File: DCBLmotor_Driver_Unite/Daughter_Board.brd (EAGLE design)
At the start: 99.8 x 72.3 mm, 40 parts, among them CN1 DF11-16DP-2DSA, CN2 26-01-3115, CN3 39-28-1023, IC1 IR25750LPBF, IC2 IR25750LPBF, IC3 IR25750LPBF, IC4 DRV8320SRTVT

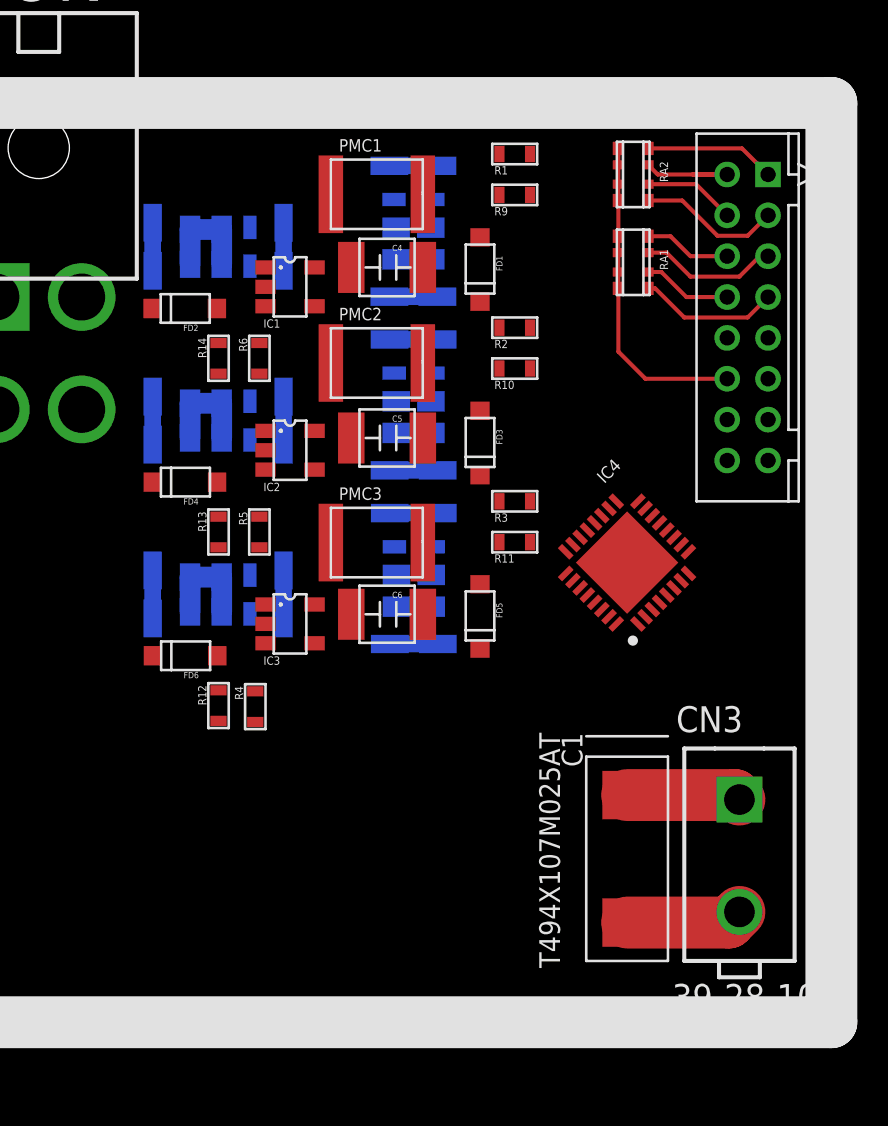
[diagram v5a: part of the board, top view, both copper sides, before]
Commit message: Build around FET
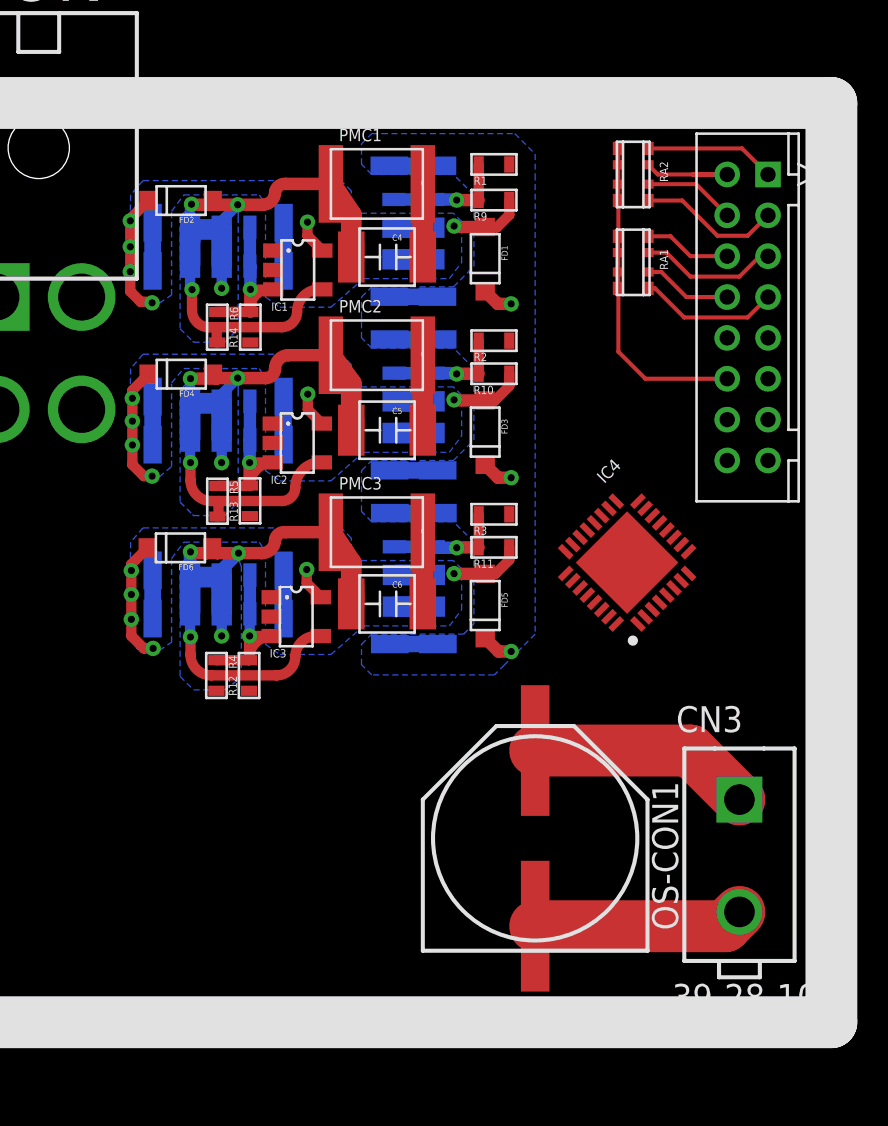
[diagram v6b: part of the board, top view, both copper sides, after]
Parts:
- removed C1: T494X107M025AT, KEMET:T494_X
- added OS-CON1: 50SVPF68M, OS-CON:F12
- moved FD6 5.29 mm to (34.5, 46.2)
- moved FD2 5.29 mm to (34.6, 63.2)
- moved FD4 5.29 mm to (34.6, 54.7)
- moved R5 1.59 mm to (39.5, 48.5)
- moved R6 1.59 mm to (39.6, 57.0)
- moved R4 1.55 mm to (39.5, 40.0)
- moved R14 1.53 mm to (37.9, 57.0), turned to 90 degrees
- moved R13 1.50 mm to (37.9, 48.5), turned to 90 degrees
- moved R12 1.48 mm to (37.9, 40.0), turned to 90 degrees
- moved R2 1.20 mm to (51.5, 56.4)
- moved R3 1.20 mm to (51.5, 47.9)
- moved R1 1.14 mm to (51.5, 65.0)
- moved R10 1.05 mm to (51.5, 54.7)
- moved R11 1.05 mm to (51.5, 46.2)
- moved R9 1.05 mm to (51.5, 63.2)
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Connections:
- removed net N$6: IC1.P$3, R14.P$2
- net GND: now also IC1.P$4, OS-CON1.P$-, R14.P$1; no longer C1.P$2
- net N$4: now also IC1.P$3, R14.P$2
- net VCC: now also OS-CON1.P$+; no longer C1.P$+
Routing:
- net GND: track 20.6 -> 106.7 mm, vias 0 -> 12
- net VCC: track 19.7 -> 40.5 mm, vias 0 -> 3
- net VS1: track 4.70 -> 19.6 mm, vias 0 -> 6
- net VS2: track 4.70 -> 19.5 mm, vias 0 -> 6
- net VS3: track 4.70 -> 19.3 mm, vias 0 -> 6
- net N$18: track 0.00 -> 8.53 mm, vias 0 -> 1
- net N$2: track 0.00 -> 8.48 mm, vias 0 -> 1
- net N$4: track 0.00 -> 8.35 mm, vias 0 -> 1
- net N$21: track 0.00 -> 5.90 mm, vias 0 -> 1
- net N$20: track 0.00 -> 5.77 mm, vias 0 -> 1
- net N$19: track 0.00 -> 5.77 mm, vias 0 -> 1
- added copper zone on layer 16, net GND
- added copper zone on layer 2, net GND
- added copper zone on layer 16, net VCC
- added copper zone on layer 16, net VS1
- added copper zone on layer 16, net VS2
- added copper zone on layer 16, net VS3

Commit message: Just before Delete MCU from daughter
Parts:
- removed CN1: DF11-16DP-2DSA, Hirose:DF11-16DP-2D
- removed CN3: 39-28-1023, Molex:39-28-1023
- removed R10, R11, R12, R13, R14, R9: ESR03EZPJ753, ROHM:ESR03
- removed RA1, RA2: EXB-38V103JV, Pana_Chip_RA:EXB-38V,28V
- added C1, C2: CKG32KX7R1H105M335AJ, TDK:CGK32K
- added C10, C11: GRM0225C1E120JA03L, murata:0402
- added C3: CGA2B3X7R1H473K050BB, TDK:C0402
- added C7: 337CKS063M, Cornell Dubilier:10
- added C8, C9: GRM035R60J475ME15D, murata:0603
- added CN4: DF63-3P-3.96DSA, Hirose:DF63-3P-3.96DSA
- added DC1, DC2, DC3, DC4: YFF15PC1C104MT000N, TDK:YFF15PC
- added IC6: LTM8050IY#PBF-ND, LTM8050IY#PBF-ND:BGA70C127P7X11_900X1500X512
- added IC7: TMPM373FWDUG, TMPM373FWDUG:QFP50P900X900X160-48N
- added XTAL1: ABM8AIG-10.000MHZ-12-2Z-T3, Abracon:ABM8AIG
- CN2: value 26-01-3115 -> DF63-2P-3.96DSA; device Molex:26-01-3115 -> Hirose:DF63-2P-3.96DSA
- OS-CON1: value 50SVPF68M -> 63SXE33M; device OS-CON:F12 -> OS-CON:E12
- moved CN2 19.5 mm to (30.4, 39.0), turned to 90 degrees
- moved IC4 13.8 mm to (62.9, 58.4), turned to 45 degrees
- moved OS-CON1 13.4 mm to (40.6, 28.3), turned to 270 degrees
- moved FD6 1.54 mm to (36.1, 46.0)
- moved FD4 1.46 mm to (36.0, 54.5)
- moved FD2 1.43 mm to (36.0, 63.0)
- moved C6 0.05 mm to (48.1, 43.5)
- moved PMC3 0.05 mm to (48.1, 47.0)
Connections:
- removed net +5V: CN1.P$16
- removed net GND_LG: CN1.P$12, RA1.P$5, RA1.P$6, RA1.P$7, RA1.P$8, RA2.P$5, RA2.P$6, RA2.P$7, RA2.P$8
- new net +3.3V: C2.P$2, DC1.P$1, DC2.P$2, DC4.P$2, IC4.24, IC6.A1, IC6.A2, IC6.A3, IC6.A4, IC6.B1, IC6.B2, IC6.B3, IC6.B4, IC6.C1, IC6.C2, IC6.C3, IC6.C4, IC6.D1, IC6.D2, IC6.D3, IC6.D4
- new net AGND: C2.P$1, IC4.23, IC4.31
- new net N$10: DC1.P$2, IC7.11
- new net N$14: C9.P$1, IC7.33
- new net N$3: C11.P$1, IC7.27, XTAL1.P$3
- new net N$5: C1.P$2, IC4.2
- new net N$6: DC2.P$1, IC7.32
- new net N$7: C3.P$2, IC4.1
- new net N$8: C3.P$1, IC4.32
- new net N$9: DC4.P$1, IC7.26
- net CU1: now also IC1.P$1, IC7.39; no longer CN1.P$15
- net CU2: now also IC2.P$1, IC7.40; no longer CN1.P$14
- net CU3: now also IC3.P$1, IC7.41; no longer CN1.P$13
- net GND: now also C10.P$2, C11.P$2, C7.P$-, C8.P$2, C9.P$2, CN2.P$1, DC1.P$3, DC1.P$4, DC2.P$3, DC2.P$4, DC4.P$3, DC4.P$4, IC4.16, IC4.33, IC4.8, IC4.9, IC6.A5, IC6.A6, IC6.A7, IC6.B5, IC6.B6, IC6.B7, IC6.C5, IC6.C6, IC6.C7, IC6.D5, IC6.D6, IC6.D7, IC6.E1, IC6.E2, IC6.E3, IC6.E4, IC6.E5, IC6.E6, IC6.E7, IC6.F1, IC6.F2, IC6.F3, IC6.F4, IC6.F5, IC6.F6, IC6.F7, IC6.G1, IC6.G2, IC6.G3, IC6.G4, IC6.G6, IC6.H6, IC6.J5, IC6.J6, IC6.K5, IC6.K6, IC6.L7, IC7.10, IC7.28; no longer CN3.P$2, R12.P$1, R13.P$1, R14.P$1
- net HIN1: now also IC4.25, IC7.2; no longer CN1.P$3, RA2.P$4
- net HIN2: now also IC4.27, IC7.4; no longer CN1.P$5, RA1.P$2
- net HIN3: now also IC4.29, IC7.6; no longer CN1.P$7, RA1.P$4
- net HO1: now also IC4.5
- net HO2: now also IC4.12
- net HO3: now also IC4.13
- net LIN1: now also IC4.26, IC7.3; no longer CN1.P$4, RA2.P$3
- net LIN2: now also IC4.28, IC7.5; no longer CN1.P$6, RA1.P$1
- net LIN3: now also IC4.30, IC7.7; no longer CN1.P$8, RA1.P$3
- net LO1: now also IC4.7
- net LO2: now also IC4.10
- net LO3: now also IC4.15
- net N$1: now also C10.P$1, IC7.29, XTAL1.P$1; no longer CN1.P$1, RA2.P$1
- net N$11: now also DC3.P$1, IC7.43; no longer CN1.P$9
- net N$12: now also DC3.P$3, DC3.P$4, IC7.42; no longer CN1.P$10
- net N$13: now also C8.P$1, IC7.30; no longer CN1.P$11
- net N$18: no longer R12.P$2
- net N$19: no longer R11.P$1
- net N$2: no longer R13.P$2
- net N$20: no longer R10.P$1
- net N$21: no longer R9.P$1
- net N$4: no longer R14.P$2
- net SD: now also IC4.22; no longer CN1.P$2, RA2.P$2
- net VCC: now also C1.P$1, C7.P$+, CN2.P$2, IC4.3, IC4.4, IC6.J1, IC6.J2, IC6.J3, IC6.J7, IC6.K1, IC6.K2, IC6.K3, IC6.L1, IC6.L2, IC6.L3; no longer CN3.P$1
- net VS1: now also CN4.P$1, IC4.6; no longer CN2.P$2, R9.P$2
- net VS2: now also CN4.P$2, IC4.11; no longer CN2.P$3, R10.P$2
- net VS3: now also CN4.P$3, IC4.14; no longer CN2.P$1, R11.P$2
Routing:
- net GND: track 106.7 -> 271.5 mm, vias 12 -> 27
- net VCC: track 40.5 -> 110.0 mm, vias 3 -> 15
- net CU1: track 0.00 -> 60.0 mm
- net CU2: track 0.00 -> 50.6 mm, vias 0 -> 2
- net CU3: track 0.00 -> 41.3 mm, vias 0 -> 2
- net LO3: track 0.00 -> 40.7 mm
- net LO2: track 0.00 -> 32.0 mm, vias 0 -> 2
- net LIN2: track 4.28 -> 32.4 mm, vias 0 -> 2
- net LIN1: track 4.51 -> 30.7 mm, vias 0 -> 2
- net LO1: track 0.00 -> 25.8 mm
- net HIN2: track 6.78 -> 31.7 mm, vias 0 -> 2
- net VS3: track 19.3 -> 42.1 mm
- net N$3: track 0.00 -> 22.5 mm
- net HIN1: track 7.00 -> 28.9 mm, vias 0 -> 2
- net AGND: track 0.00 -> 19.8 mm
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- added copper zone on layer 16, net +3.3V
- added copper zone on layer 3, net +3.3V
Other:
- board text removed: "+20V Output"

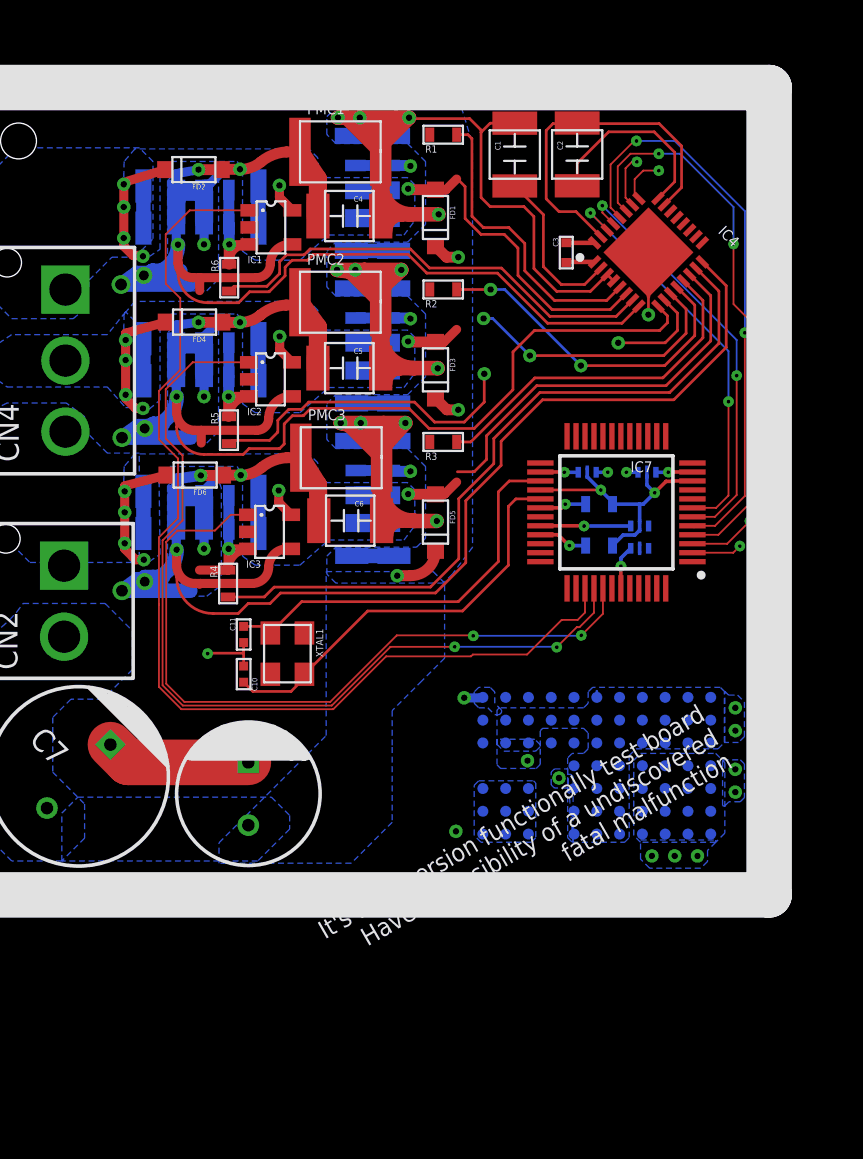
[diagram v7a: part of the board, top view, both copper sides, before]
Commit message: Attach DC-DC Converter
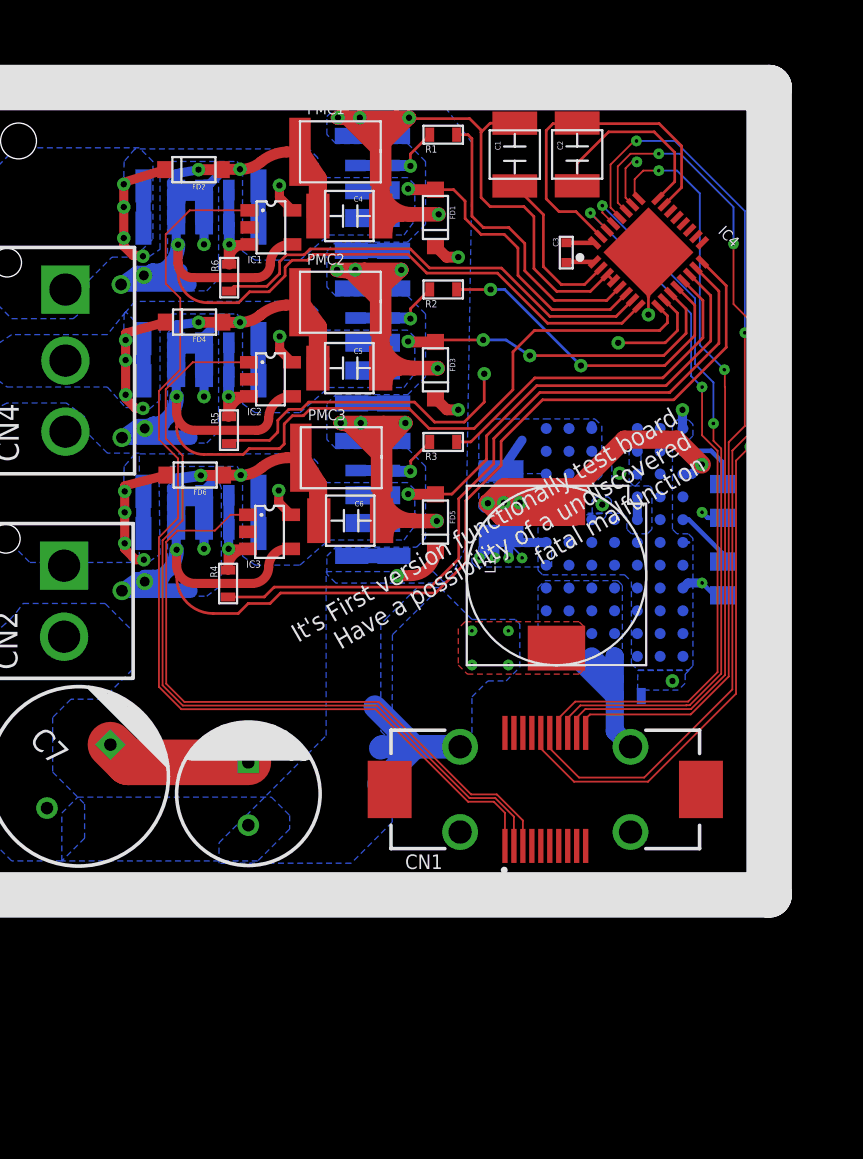
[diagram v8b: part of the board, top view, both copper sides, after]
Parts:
- removed C10, C11: GRM0225C1E120JA03L, murata:0402
- removed DC1, DC2, DC3, DC4: YFF15PC1C104MT000N, TDK:YFF15PC
- removed IC7: TMPM373FWDUG, TMPM373FWDUG:QFP50P900X900X160-48N
- removed XTAL1: ABM8AIG-10.000MHZ-12-2Z-T3, Abracon:ABM8AIG
- added CN1: FX23L-20P-0.5SV12, FX23L-20P-0.5SV12:FX23L-20P-0.5SV12
- added L1: SLF10145T-470M1R4-PF, TDK:SLF10145
- added R7: ERA-6AEB9312V, Panasonic:R0805
- added R8: ERA-6AEB5762V, Panasonic:R0805
- C8: value GRM035R60J475ME15D -> CGA6M3X7S2A475M200AB; device murata:0603 -> TDK:C1210
- moved IC6 12.5 mm to (61.0, 42.3), turned to 180 degrees
- moved C9 8.53 mm to (61.8, 33.7), turned to 0 degrees
- moved C8 5.46 mm to (54.7, 44.5), turned to 90 degrees
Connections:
- removed net N$10: DC1.P$2, IC7.11
- removed net N$11: DC3.P$1, IC7.43
- removed net N$12: DC3.P$3, DC3.P$4, IC7.42
- removed net N$13: C8.P$1, IC7.30
- removed net N$14: C9.P$1, IC7.33
- removed net N$9: DC4.P$1, IC7.26
- new net +5V: C9.P$2, CN1.25, IC6.A1, IC6.A2, IC6.A3, IC6.A4, IC6.B1, IC6.B2, IC6.B3, IC6.B4, IC6.C1, IC6.C2, IC6.C3, IC6.C4, IC6.D1, IC6.D2, IC6.D3, IC6.D4
- new net IN_A: C8.P$2, IC6.J1, IC6.J2, IC6.J3, IC6.J7, IC6.K1, IC6.K2, IC6.K3, IC6.L1, IC6.L2, IC6.L3, L1.P$1
- net +3.3V: no longer DC1.P$1, DC2.P$2, DC4.P$2, IC6.A1, IC6.A2, IC6.A3, IC6.A4, IC6.B1, IC6.B2, IC6.B3, IC6.B4, IC6.C1, IC6.C2, IC6.C3, IC6.C4, IC6.D1, IC6.D2, IC6.D3, IC6.D4
- net CU1: now also CN1.1; no longer IC7.39
- net CU2: now also CN1.2; no longer IC7.40
- net CU3: now also CN1.3; no longer IC7.41
- net GND: now also C8.P$1, C9.P$1, CN1.24, R7.2, R8.2; no longer C10.P$2, C11.P$2, C8.P$2, C9.P$2, DC1.P$3, DC1.P$4, DC2.P$3, DC2.P$4, DC4.P$3, DC4.P$4, IC7.10, IC7.28
- net HIN1: now also CN1.19; no longer IC7.2
- net HIN2: now also CN1.16; no longer IC7.4
- net HIN3: now also CN1.18; no longer IC7.6
- net LIN1: now also CN1.15; no longer IC7.3
- net LIN2: now also CN1.20; no longer IC7.5
- net LIN3: now also CN1.17; no longer IC7.7
- net N$1: now also IC6.G5, IC6.H5; no longer C10.P$1, IC7.29, XTAL1.P$1
- net N$3: now also IC6.K7, R7.1; no longer C11.P$1, IC7.27, XTAL1.P$3
- net N$6: now also IC6.G7, R8.1; no longer DC2.P$1, IC7.32
- net VCC: now also CN1.23, L1.P$2; no longer IC6.J1, IC6.J2, IC6.J3, IC6.J7, IC6.K1, IC6.K2, IC6.K3, IC6.L1, IC6.L2, IC6.L3
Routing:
- net IN_A: track 0.00 -> 30.0 mm, vias 0 -> 4
- net N$1: track 23.2 -> 1.27 mm
- net LIN1: track 30.7 -> 51.5 mm
- net HIN2: track 31.7 -> 52.3 mm
- net N$3: track 22.5 -> 3.70 mm
- net LIN3: track 23.2 -> 40.6 mm
- net HIN3: track 23.5 -> 40.5 mm
- net LIN2: track 32.4 -> 48.9 mm
- net VCC: track 110.0 -> 125.6 mm, vias 15 -> 19
- net HIN1: track 28.9 -> 43.2 mm
- net +5V: track 0.00 -> 10.8 mm
- net GND: track 271.5 -> 265.6 mm, vias 27 -> 29
- net CU1: track 60.0 -> 56.2 mm
- net CU2: track 50.6 -> 46.9 mm, vias 2 -> 0
- net CU3: track 41.3 -> 37.5 mm, vias 2 -> 0
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- added copper zone on layer 16, net +5V
- added copper zone on layer 16, net IN_A
- added copper zone on layer 1, net VCC
- removed copper zone on layer 16, net +3.3V
